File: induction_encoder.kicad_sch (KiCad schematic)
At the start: 68 parts, among them J402 Conn_01x06, U1 MT9105ET, U10 IPS2200, U11 ADS1115IDGS, U12 ADS1115IDGS, U2 MT9105ET, U4 MT9105ET, U5 MT9105ET, U7 ADS1115IDGS, U8 MT9105ET

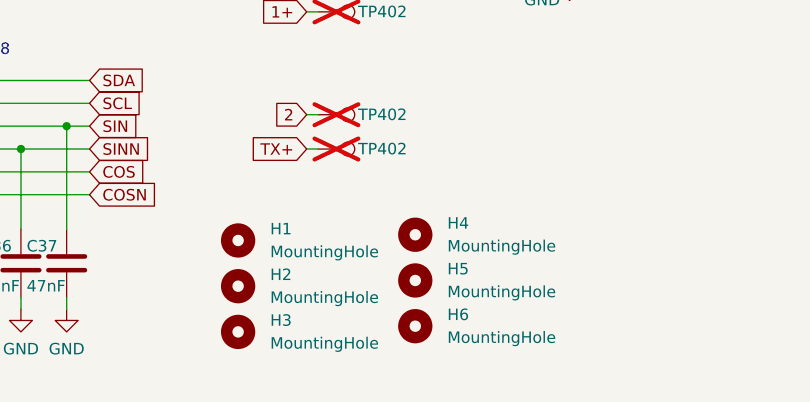
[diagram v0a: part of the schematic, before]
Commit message: initial layout for 100-170mm induction encoder
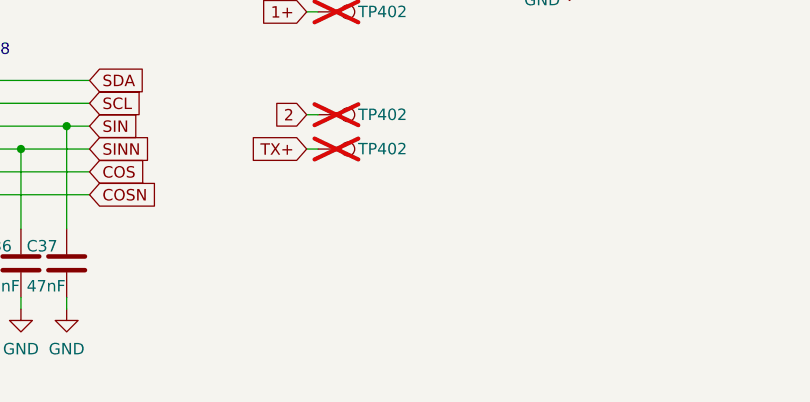
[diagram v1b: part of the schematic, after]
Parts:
- removed H1, H2, H3, H4, H5, H6: MountingHole, encoder:SMD_BD5.6-D4.1, symbol Mechanical:MountingHole

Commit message: 118-220 boards ready to order
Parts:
- removed C1: 10u, Capacitor_SMD:C_0805_2012Metric, symbol Device:C
- removed C2 (x4): 100n, Capacitor_SMD:C_0603_1608Metric, symbol Device:C
- removed C3 (x4): 4.7n, Capacitor_SMD:C_0603_1608Metric, symbol Device:C
- removed J402: Conn_01x06, parts:Ckmtw-W-2510S06P_1x06_P2.54mm_Horizontal, symbol Connector_Generic:Conn_01x06
- removed R56: 10k, Resistor_SMD:R_0603_1608Metric, symbol MotorController:TAYLOR_RESISTOR
- removed U1 (x4): MT9105ET, Package_TO_SOT_SMD:SOT-23, symbol Sensor_Magnetic:A1101LLHL
- removed U10: IPS2200, Package_SO:TSSOP-16_4.4x5mm_P0.65mm, symbol taylor_kicad:IPS2200
- added C14, C2, C21, C26: 100n, Capacitor_SMD:C_0603_1608Metric, symbol Device:C
- added C15, C22, C27, C3: 4.7n, Capacitor_SMD:C_0603_1608Metric, symbol Device:C
- added C25: 10u, Capacitor_SMD:C_0805_2012Metric, symbol Device:C
- added J2: Conn_01x06, parts:Ckmtw-W-2510S06P_1x06_P2.54mm_Horizontal, symbol Connector_Generic:Conn_01x06
- added R10: 10K, Resistor_SMD:R_0603_1608Metric, symbol Device:R
- added U1, U3, U6, U9: MT9105ET, Package_TO_SOT_SMD:SOT-23, symbol Sensor_Magnetic:A1101LLHL
- added U10: IPS2200, Package_SO:TSSOP-16_4.4x5mm_P0.65mm, symbol induction_encoder:IPS2200
- C22, C4, C6: LCSC (none) -> C14663
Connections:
- net +3V3: now also C14.1, C2.1, C21.1, C25.2, C26.1, J2.2 (Pin_2), R10.1, U1.1 (VCC), U10.10 (VDD), U3.1 (VCC), U6.1 (VCC), U9.1 (VCC)
- net 1+: now also U10.4 (RX3)
- net 1-: now also U10.5 (RX4)
- net 2: now also U10.2 (RX1), U10.3 (RX2)
- net COS: now also U10.12 (COS)
- net COSN: now also U10.11 (COSN)
- net GND: now also C14.2, C15.1, C2.2, C21.2, C22.1, C25.1, C26.2, C27.1, C3.1, J2.6 (Pin_6), U1.3 (GND), U10.9 (GND), U3.3 (GND), U6.3 (GND), U9.3 (GND)
- net MAG1: now also C27.2, U9.2 (VOUT)
- net MAG2: now also C15.2, U3.2 (VOUT)
- net MAG3: now also C22.2, U6.2 (VOUT)
- net MAG4: now also C3.2, U1.2 (VOUT)
- net RDY: now also J2.5 (Pin_5)
- net SCL: now also J2.4 (Pin_4), U10.15 (SCK_SCL)
- net SDA: now also J2.3 (Pin_3), U10.16 (SIO_SDA)
- net SIN: now also U10.14 (SIN)
- net SINN: now also U10.13 (SINN)
- net at R11.2: now also U10.6 (TX1)
- net at C38.2, C39.2: now also U10.8 (VDDA)
- net at R12.2: now also U10.7 (TX2)
- new net: R10.2, U10.1 (CSN_IRQN)
- no-connect marks 0 -> 3
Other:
- moved on the sheet: TP1
